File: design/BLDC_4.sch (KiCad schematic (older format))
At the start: 33 parts, among them K1 SERVO, P1 CANBUS, P10 MOTOR3, P11 MOTOR2, P12 MOTOR1, P2 HALL/Encoder, P3 HALL/Encoder, P4 PWR_COMM, P5 IN+, P6 IN-, P7 MOTOR3, P8 MOTOR2, P9 MOTOR1, X1 MINI-USB-SHIELD-32005-201

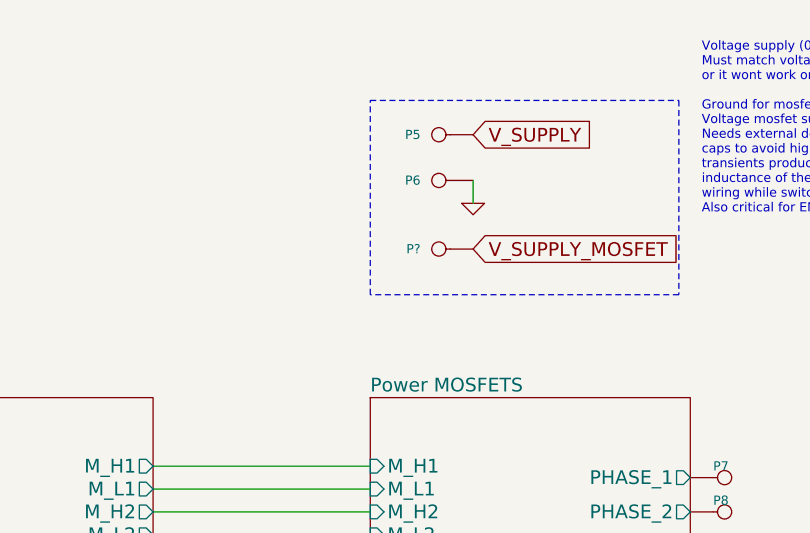
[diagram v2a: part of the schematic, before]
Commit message: Change libraries ot new pretty format
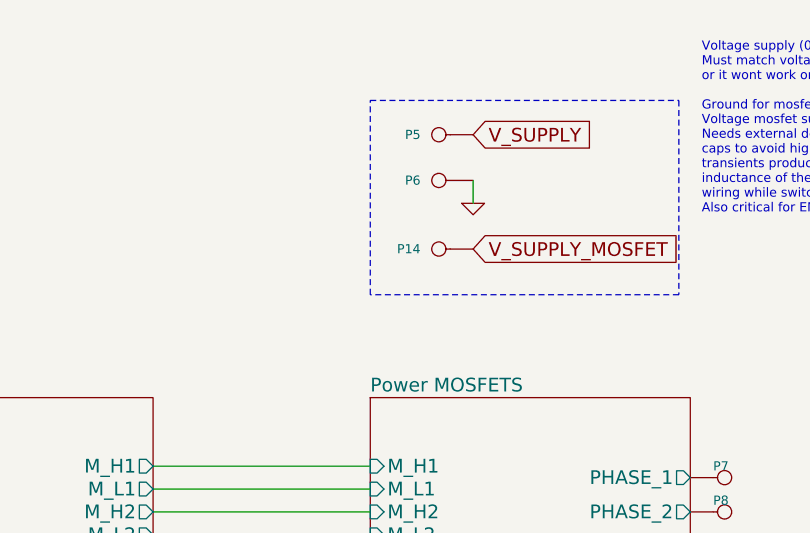
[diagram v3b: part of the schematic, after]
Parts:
- gave numbers to parts that had none: 1
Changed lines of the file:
@@
 $EndComp
 $Comp
-L +5V #PWR3
+L +5V #PWR01
 U 1 1 522DA04D
 P 2850 5050
-F 0 "#PWR3" H 2850 5140 20  0001 C CNN
+F 0 "#PWR01" H 2850 5140 20  0001 C CNN
 F 1 "+5V" V 2800 5100 30  0000 C CNN
 F 2 "" H 2850 5050 60  0001 C CNN
@@
 $EndComp
 $Comp
-L GND #PWR6
+L GND #PWR02
 U 1 1 522DA053
 P 2900 4550
-F 0 "#PWR6" H 2900 4550 30  0001 C CNN
+F 0 "#PWR02" H 2900 4550 30  0001 C CNN
 F 1 "GND" H 2900 4480 30  0001 C CNN
 F 2 "" H 2900 4550 60  0001 C CNN
@@
 $EndComp
 $Comp
-L GND #PWR18
+L GND #PWR03
 U 1 1 522DA0BA
 P 8400 6000
-F 0 "#PWR18" H 8400 6000 30  0001 C CNN
+F 0 "#PWR03" H 8400 6000 30  0001 C CNN
 F 1 "GND" H 8400 5930 30  0001 C CNN
 F 2 "" H 8400 6000 60  0001 C CNN
@@
 V_SUPPLY
 $Comp
-L GND #PWR11
+L GND #PWR04
 U 1 1 522DA0CE
 P 3100 2650
-F 0 "#PWR11" H 3100 2650 30  0001 C CNN
+F 0 "#PWR04" H 3100 2650 30  0001 C CNN
 F 1 "GND" H 3100 2580 30  0001 C CNN
 F 2 "" H 3100 2650 60  0001 C CNN
@@
 $EndComp
 $Comp
-L GND #PWR5
+L GND #PWR05
 U 1 1 522DA0E2
 P 2850 6950
-F 0 "#PWR5" H 2850 6950 30  0001 C CNN
+F 0 "#PWR05" H 2850 6950 30  0001 C CNN
 F 1 "GND" H 2850 6880 30  0001 C CNN
 F 2 "" H 2850 6950 60  0001 C CNN
@@
 $EndComp
 $Comp
-L GND #PWR10
+L GND #PWR06
 U 1 1 522DA0FC
 P 3000 3600
-F 0 "#PWR10" H 3000 3600 30  0001 C CNN
+F 0 "#PWR06" H 3000 3600 30  0001 C CNN
 F 1 "GND" H 3000 3530 30  0001 C CNN
 F 2 "" H 3000 3600 60  0001 C CNN
@@
 $EndComp
 $Comp
-L +5V #PWR8
+L +5V #PWR07
 U 1 1 522DA11A
 P 2950 6750
-F 0 "#PWR8" H 2950 6840 20  0001 C CNN
+F 0 "#PWR07" H 2950 6840 20  0001 C CNN
 F 1 "+5V" V 2950 6900 30  0000 C CNN
 F 2 "" H 2950 6750 60  0001 C CNN
@@
 $EndComp
 $Comp
-L VCC #PWR9
+L VCC #PWR08
 U 1 1 522DA120
 P 2950 6850
-F 0 "#PWR9" H 2950 6950 30  0001 C CNN
+F 0 "#PWR08" H 2950 6950 30  0001 C CNN
 F 1 "VCC" V 2950 7000 30  0000 C CNN
 F 2 "" H 2950 6850 60  0001 C CNN
@@
 $EndComp
 $Comp
-L +5V #PWR17
+L +5V #PWR09
 U 1 1 522DA158
 P 8400 5550
-F 0 "#PWR17" H 8400 5640 20  0001 C CNN
+F 0 "#PWR09" H 8400 5640 20  0001 C CNN
 F 1 "+5V" H 8400 5640 30  0000 C CNN
 F 2 "" H 8400 5550 60  0001 C CNN
@@
 $EndComp
 $Comp
-L +5V #PWR12
+L +5V #PWR010
 U 1 1 522DA254
 P 4200 3050
-F 0 "#PWR12" H 4200 3140 20  0001 C CNN
+F 0 "#PWR010" H 4200 3140 20  0001 C CNN
 F 1 "+5V" H 4200 3140 30  0000 C CNN
 F 2 "" H 4200 3050 60  0001 C CNN
@@
 $EndComp
 $Comp
-L GND #PWR26
+L GND #PWR011
 U 1 1 53FA1F8F
 P 10850 6200
-F 0 "#PWR26" H 10850 6200 30  0001 C CNN
+F 0 "#PWR011" H 10850 6200 30  0001 C CNN
 F 1 "GND" H 10850 6130 30  0001 C CNN
 F 2 "" H 10850 6200 60  0001 C CNN
@@
 C8 C8 08 D2 A9 87 39 1B F9 3D 64 10 3C A5 22 3B 19 76 2F 98 2B 2B 2B 1E 8F A7 AB AB 0B FB AC 1D
 B9 73 C8 EF 2C EC 8D 33 57 03 96 70 05 29 43 0C 6A C5 A8 D7 30 9E 87 2D DE BE E8 EA 73 2F 9C 18
-F1 B3 C3 9F 6D FA 1E FF 03 71 17 46 7E 55 DF FF 4E 00 00 00 00 49 45 4E 44 AE 42 60 82 1A $EndBitmap
+F1 B3 C3 9F 6D FA 1E FF 03 71 17 46 7E 55 DF FF 4E 00 00 00 00 49 45 4E 44 AE 42 60 82 DB $EndBitmap
 EndData
 $EndBitmap
@@
 $EndSheet
 $Comp
-L GND #PWR2
+L GND #PWR012
 U 1 1 53FB6DA8
 P 2850 4200
-F 0 "#PWR2" H 2850 4200 30  0001 C CNN
+F 0 "#PWR012" H 2850 4200 30  0001 C CNN
 F 1 "GND" H 2850 4130 30  0001 C CNN
 F 2 "" H 2850 4200 60  0001 C CNN
@@
 $EndComp
 $Comp
-L GND #PWR13
+L GND #PWR013
 U 1 1 53FC021C
 P 7300 7200
-F 0 "#PWR13" H 7300 7200 30  0001 C CNN
+F 0 "#PWR013" H 7300 7200 30  0001 C CNN
 F 1 "GND" H 7300 7130 30  0001 C CNN
 F 2 "" H 7300 7200 60  0001 C CNN
@@
 $EndComp
 $Comp
-L GND #PWR14
+L GND #PWR014
 U 1 1 53FC131A
 P 7600 7200
-F 0 "#PWR14" H 7600 7200 30  0001 C CNN
+F 0 "#PWR014" H 7600 7200 30  0001 C CNN
 F 1 "GND" H 7600 7130 30  0001 C CNN
 F 2 "" H 7600 7200 60  0001 C CNN
@@
 $EndComp
 $Comp
-L GND #PWR16
+L GND #PWR015
 U 1 1 53FC8AA4
 P 7900 7200
-F 0 "#PWR16" H 7900 7200 30  0001 C CNN
+F 0 "#PWR015" H 7900 7200 30  0001 C CNN
 F 1 "GND" H 7900 7130 30  0001 C CNN
 F 2 "" H 7900 7200 60  0001 C CNN
@@
 $EndComp
 $Comp
-L VCC #PWR15
+L VCC #PWR016
 U 1 1 53FC98D2
 P 7900 6300
-F 0 "#PWR15" H 7900 6400 30  0001 C CNN
+F 0 "#PWR016" H 7900 6400 30  0001 C CNN
 F 1 "VCC" V 7900 6450 30  0000 C CNN
 F 2 "" H 7900 6300 60  0001 C CNN
@@
 $EndComp
 $Comp
-L +5V #PWR1
+L +5V #PWR017
 U 1 1 54036995
 P 2850 3900
-F 0 "#PWR1" H 2850 3990 20  0001 C CNN
+F 0 "#PWR017" H 2850 3990 20  0001 C CNN
 F 1 "+5V" H 2850 3990 30  0000 C CNN
 F 2 "" H 2850 3900 60  0001 C CNN
@@
 $EndComp
 $Comp
-L GND #PWR27
+L GND #PWR018
 U 1 1 548F24DF
 P 11150 6200
-F 0 "#PWR27" H 11150 6200 30  0001 C CNN
+F 0 "#PWR018" H 11150 6200 30  0001 C CNN
 F 1 "GND" H 11150 6130 30  0001 C CNN
 F 2 "" H 11150 6200 60  0001 C CNN
@@
 $EndComp
 $Comp
-L GND #PWR23
+L GND #PWR019
 U 1 1 548F2504
 P 9850 5250
-F 0 "#PWR23" H 9850 5250 30  0001 C CNN
+F 0 "#PWR019" H 9850 5250 30  0001 C CNN
 F 1 "GND" H 9850 5180 30  0001 C CNN
 F 2 "" H 9850 5250 60  0001 C CNN
@@
 $EndComp
 $Comp
-L GND #PWR19
+L GND #PWR020
 U 1 1 548F2529
 P 9550 4750
-F 0 "#PWR19" H 9550 4750 30  0001 C CNN
+F 0 "#PWR020" H 9550 4750 30  0001 C CNN
 F 1 "GND" H 9550 4680 30  0001 C CNN
 F 2 "" H 9550 4750 60  0001 C CNN
@@
 $EndComp
 $Comp
-L GND #PWR21
+L GND #PWR021
 U 1 1 548F254E
 P 9700 4250
-F 0 "#PWR21" H 9700 4250 30  0001 C CNN
+F 0 "#PWR021" H 9700 4250 30  0001 C CNN
 F 1 "GND" H 9700 4180 30  0001 C CNN
 F 2 "" H 9700 4250 60  0001 C CNN
@@
 $EndComp
 $Comp
-L GND #PWR25
+L GND #PWR022
 U 1 1 548F2573
 P 10500 1650
-F 0 "#PWR25" H 10500 1650 30  0001 C CNN
+F 0 "#PWR022" H 10500 1650 30  0001 C CNN
 F 1 "GND" H 10500 1580 30  0001 C CNN
 F 2 "" H 10500 1650 60  0001 C CNN
@@
 $EndComp
 $Comp
-L +5V #PWR4
+L +5V #PWR023
 U 1 1 54B6A9FD
 P 2850 6100
-F 0 "#PWR4" H 2850 6190 20  0001 C CNN
+F 0 "#PWR023" H 2850 6190 20  0001 C CNN
 F 1 "+5V" V 2800 6150 30  0000 C CNN
 F 2 "" H 2850 6100 60  0001 C CNN
@@
 $EndComp
 $Comp
-L GND #PWR7
+L GND #PWR024
 U 1 1 54B6AA03
 P 2900 5600
-F 0 "#PWR7" H 2900 5600 30  0001 C CNN
+F 0 "#PWR024" H 2900 5600 30  0001 C CNN
 F 1 "GND" H 2900 5530 30  0001 C CNN
 F 2 "" H 2900 5600 60  0001 C CNN
@@
 C8 C8 08 D2 A9 87 39 1B F9 3D 64 10 3C A5 22 3B 19 76 2F 98 2B 2B 2B 1E 8F A7 AB AB 0B FB AC 1D
 B9 73 C8 EF 2C EC 8D 33 57 03 96 70 05 29 43 0C 6A C5 A8 D7 30 9E 87 2D DE BE E8 EA 73 2F 9C 18
-F1 B3 C3 9F 6D FA 1E FF 03 71 17 46 7E 55 DF FF 4E 00 00 00 00 49 45 4E 44 AE 42 60 82 1A $EndBitmap
+F1 B3 C3 9F 6D FA 1E FF 03 71 17 46 7E 55 DF FF 4E 00 00 00 00 49 45 4E 44 AE 42 60 82 DB $EndBitmap
 EndData
 $EndBitmap
@@
 $EndComp
 $Comp
-L GND #PWR24
+L GND #PWR025
 U 1 1 54B73612
 P 9850 10800
-F 0 "#PWR24" H 9850 10800 30  0001 C CNN
+F 0 "#PWR025" H 9850 10800 30  0001 C CNN
 F 1 "GND" H 9850 10730 30  0001 C CNN
 F 2 "" H 9850 10800 60  0001 C CNN
@@
 $EndComp
 $Comp
-L GND #PWR20
+L GND #PWR026
 U 1 1 54B73618
 P 9550 10300
-F 0 "#PWR20" H 9550 10300 30  0001 C CNN
+F 0 "#PWR026" H 9550 10300 30  0001 C CNN
 F 1 "GND" H 9550 10230 30  0001 C CNN
 F 2 "" H 9550 10300 60  0001 C CNN
@@
 $EndComp
 $Comp
-L GND #PWR22
+L GND #PWR027
 U 1 1 54B7361E
 P 9700 9800
-F 0 "#PWR22" H 9700 9800 30  0001 C CNN
+F 0 "#PWR027" H 9700 9800 30  0001 C CNN
 F 1 "GND" H 9700 9730 30  0001 C CNN
 F 2 "" H 9700 9800 60  0001 C CNN
@@
 Voltage supply (0-60v)\nMust match voltage divder\nor it wont work or vice versa\n\nGround for mosfet and electronics is same
 $Comp
-L CONN_1 P?
+L CONN_1 P14
 U 1 1 54D705F4
 P 10350 1850
-F 0 "P?" H 10430 1850 40  0000 L CNN
+F 0 "P14" H 10430 1850 40  0000 L CNN
 F 1 "IN+" H 10350 1905 30  0001 C CNN
 F 2 "CRF1:1PAD_4x5mm" H 10350 1850 60  0001 C CNN

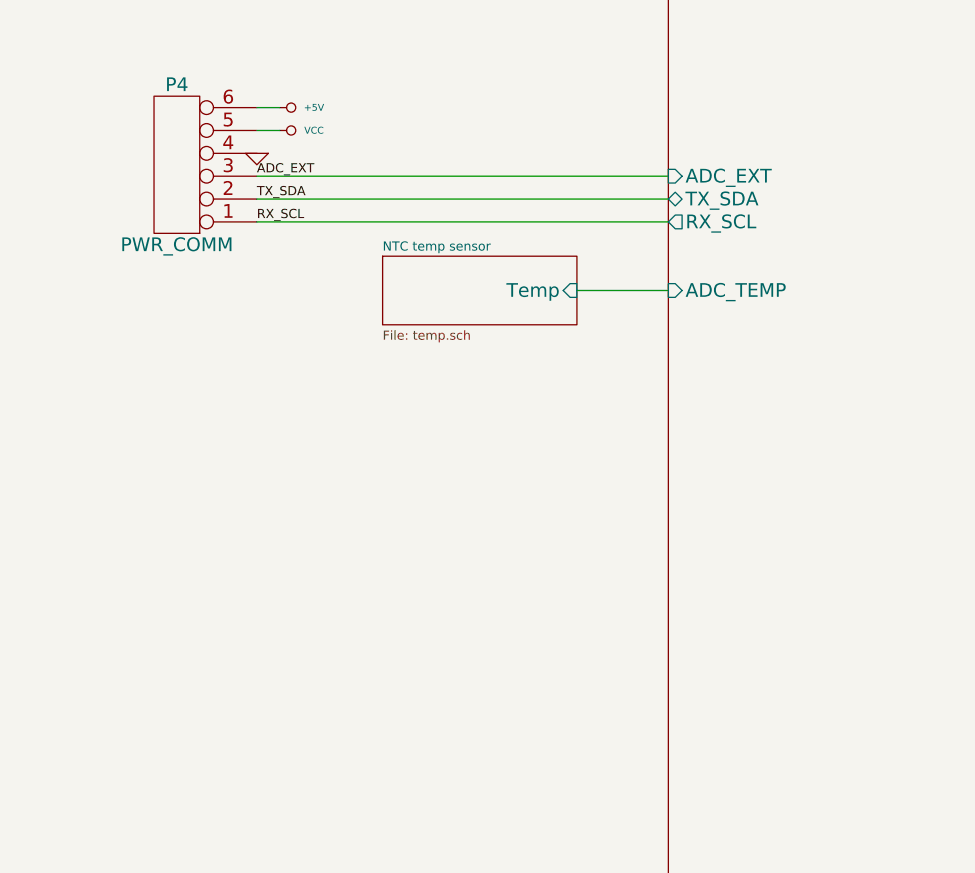
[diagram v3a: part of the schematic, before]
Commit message: Add pwr for second motor
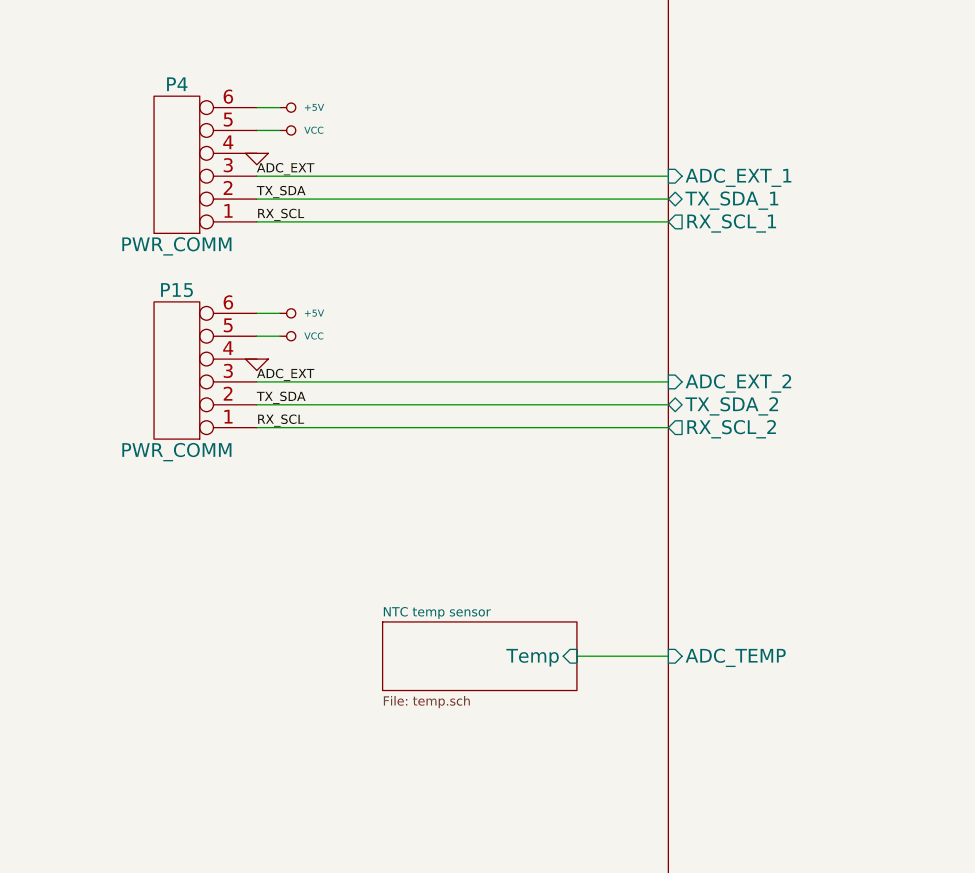
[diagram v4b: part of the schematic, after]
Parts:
- added P15: PWR_COMM, CRF1:MICRO_JST_6, symbol CONN_6
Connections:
- net +5V: now also P15.6
- net ADC_EXT: now also P15.3
- net GND: now also P15.4
- net RX_SCL: now also P15.1
- net TX_SDA: now also P15.2
- net VCC: now also P15.5

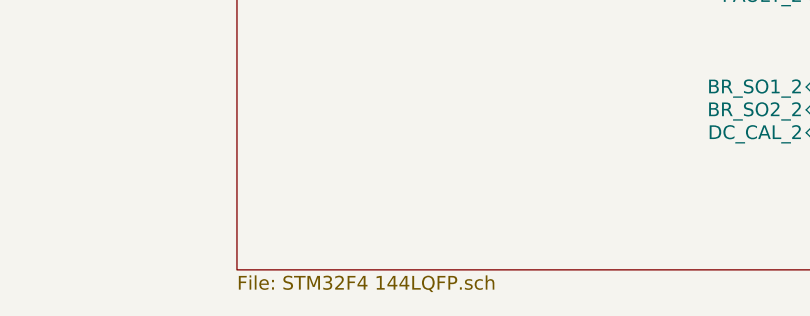
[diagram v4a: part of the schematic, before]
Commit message: Voltage divider for DRV and MCU
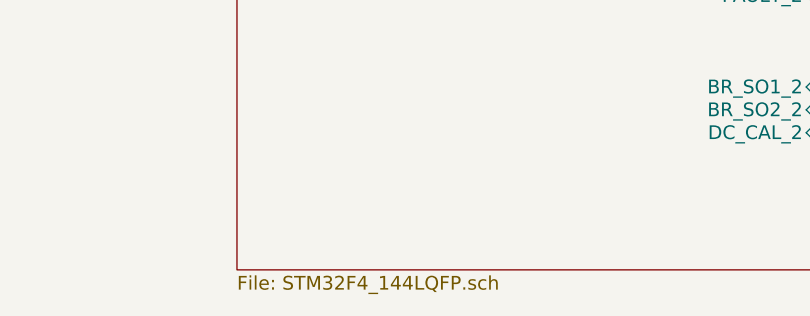
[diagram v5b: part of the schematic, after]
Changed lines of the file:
@@
 $Descr A3 16535 11693
 encoding utf-8
-Sheet 1 10
+Sheet 1 28
 Title "BLDC Driver 4.6"
 Date "6 feb 2015"
@@
 C8 C8 08 D2 A9 87 39 1B F9 3D 64 10 3C A5 22 3B 19 76 2F 98 2B 2B 2B 1E 8F A7 AB AB 0B FB AC 1D
 B9 73 C8 EF 2C EC 8D 33 57 03 96 70 05 29 43 0C 6A C5 A8 D7 30 9E 87 2D DE BE E8 EA 73 2F 9C 18
-F1 B3 C3 9F 6D FA 1E FF 03 71 17 46 7E 55 DF FF 4E 00 00 00 00 49 45 4E 44 AE 42 60 82 02
+F1 B3 C3 9F 6D FA 1E FF 03 71 17 46 7E 55 DF FF 4E 00 00 00 00 49 45 4E 44 AE 42 60 82 0C
 EndData
 $EndBitmap
@@
 C8 C8 08 D2 A9 87 39 1B F9 3D 64 10 3C A5 22 3B 19 76 2F 98 2B 2B 2B 1E 8F A7 AB AB 0B FB AC 1D
 B9 73 C8 EF 2C EC 8D 33 57 03 96 70 05 29 43 0C 6A C5 A8 D7 30 9E 87 2D DE BE E8 EA 73 2F 9C 18
-F1 B3 C3 9F 6D FA 1E FF 03 71 17 46 7E 55 DF FF 4E 00 00 00 00 49 45 4E 44 AE 42 60 82 02
+F1 B3 C3 9F 6D FA 1E FF 03 71 17 46 7E 55 DF FF 4E 00 00 00 00 49 45 4E 44 AE 42 60 82 0C
 EndData
 $EndBitmap
@@
 U 53F7501A
 F0 "MCU" 60
-F1 "STM32F4 144LQFP.sch" 60
+F1 "STM32F4_144LQFP.sch" 60
 F2 "USB_DM" T L 4650 3200 60
 F3 "USB_DP" T L 4650 3300 60
